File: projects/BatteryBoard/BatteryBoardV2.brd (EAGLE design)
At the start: 90.5 x 96 mm, 220 parts, among them M1 BSO201SP, SW1 BTS50015-1TAD, SW2 BTS50015-1TAD, T1 AD590FLATPACK, T2 AD590FLATPACK, T3 AD590FLATPACK, T4 AD590FLATPACK, U1 TCA9535PWR, U10 LT1962-3, U11 LT1962-3, U12 LTC4411, U13 LTC4411, U14 LTC4121, U15 VNS3NV04DP-E, U16 LTC4121, U17 VNS3NV04DP-E, U18 AD8418, U19 AD8418, U2 AD7991-0, U3 LTC4412MPS6, U4 LTC4121-4.2, U5 LTC4121-4.2, U6 LC05111C13MTTTG, U7 LC05111C13MTTTG, U8 AD8418, U9 AD8418

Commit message: Addition of zener diodes. Updates to some resistor values. Inital layout of all Li-ion circuitry.
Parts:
- removed V32: L2_ST, BrownSpaceEngineering:VIA-60MIL
- added D4, D5: SMBJ5343B, BattBoard:DO214AA
- added V40: LFB1SNS, BrownSpaceEngineering:VIA-60MIL
- added V44: LFB2SNS, BrownSpaceEngineering:VIA-60MIL
- R39: value 150K -> 15K
- R40: value 100K -> 10K
- R41, R59: value 0.002R@1W -> 0.001R@1W
- R42, R43, R60, R61: value 10K -> 470K
- R56, R57, R74, R75: value 10K -> 100K
- V31: value L1_ST -> L2_REF
- V33: value L_OUT -> L2_CHG; device BrownSpaceEngineering:VIA-120MIL -> BrownSpaceEngineering:VIA-60MIL
- V53: value LIFE_B2 -> LF_B2
- moved U19 237.8 mm to (86.7, 102.4), turned to 270 degrees
- moved R29 234.7 mm to (83.2, 102.1), turned to 270 degrees
- moved R30 230.3 mm to (83.2, 98.4), turned to 270 degrees
- moved R24 225.4 mm to (94.4, 85.7), turned to 270 degrees
- moved U18 225.3 mm to (99.1, 81.6), turned to 270 degrees
- moved R26 221.4 mm to (94.4, 82.0), turned to 270 degrees
- moved F1 174.5 mm to (29.8, 7.00), flipped to the bottom
- moved V42 164.5 mm to (101.3, 29.9)
- moved R8 151.8 mm to (-0.10, 73.5), flipped to the bottom, turned to 180 degrees
- moved V21 150.9 mm to (53.9, 4.60)
- moved R9 150.3 mm to (6.50, 14.1), turned to 180 degrees
- moved C13 149.7 mm to (-3.40, 79.5), flipped to the bottom, turned to 180 degrees
- moved R4 149.7 mm to (9.90, 68.5), turned to 90 degrees
- moved U6 148.2 mm to (0.80, 77.6), flipped to the bottom
- moved V20 147.8 mm to (47.9, 6.50), turned to 270 degrees
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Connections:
- net LIFE_B2 renamed LF_B2
- new net LFB1_SNS+: LIFEPO42.MINUS, R41.P$2, U18.P$8
- new net LFB2_SNS+: LIFEPO44.MINUS, R59.P$2, U19.P$8
- net GND: now also D4.A, D5.A
- net L1_SNS+: no longer LIFEPO42.MINUS, LIFEPO44.MINUS, R41.P$2, R59.P$2, U18.P$8, U19.P$8
- net L1_ST: no longer V31.P$1
- net L2_CHG: now also V33.P$1
- net L2_REF: now also V31.P$1
- net L2_ST: no longer V32.P$1
- net LF_B1_SNS: now also V40.P$1
- net LF_B2_SNS: now also V44.P$1
- net LIFE1: now also D4.C
- net LIFE3: now also D5.C
- net L_OUT: no longer V33.P$1

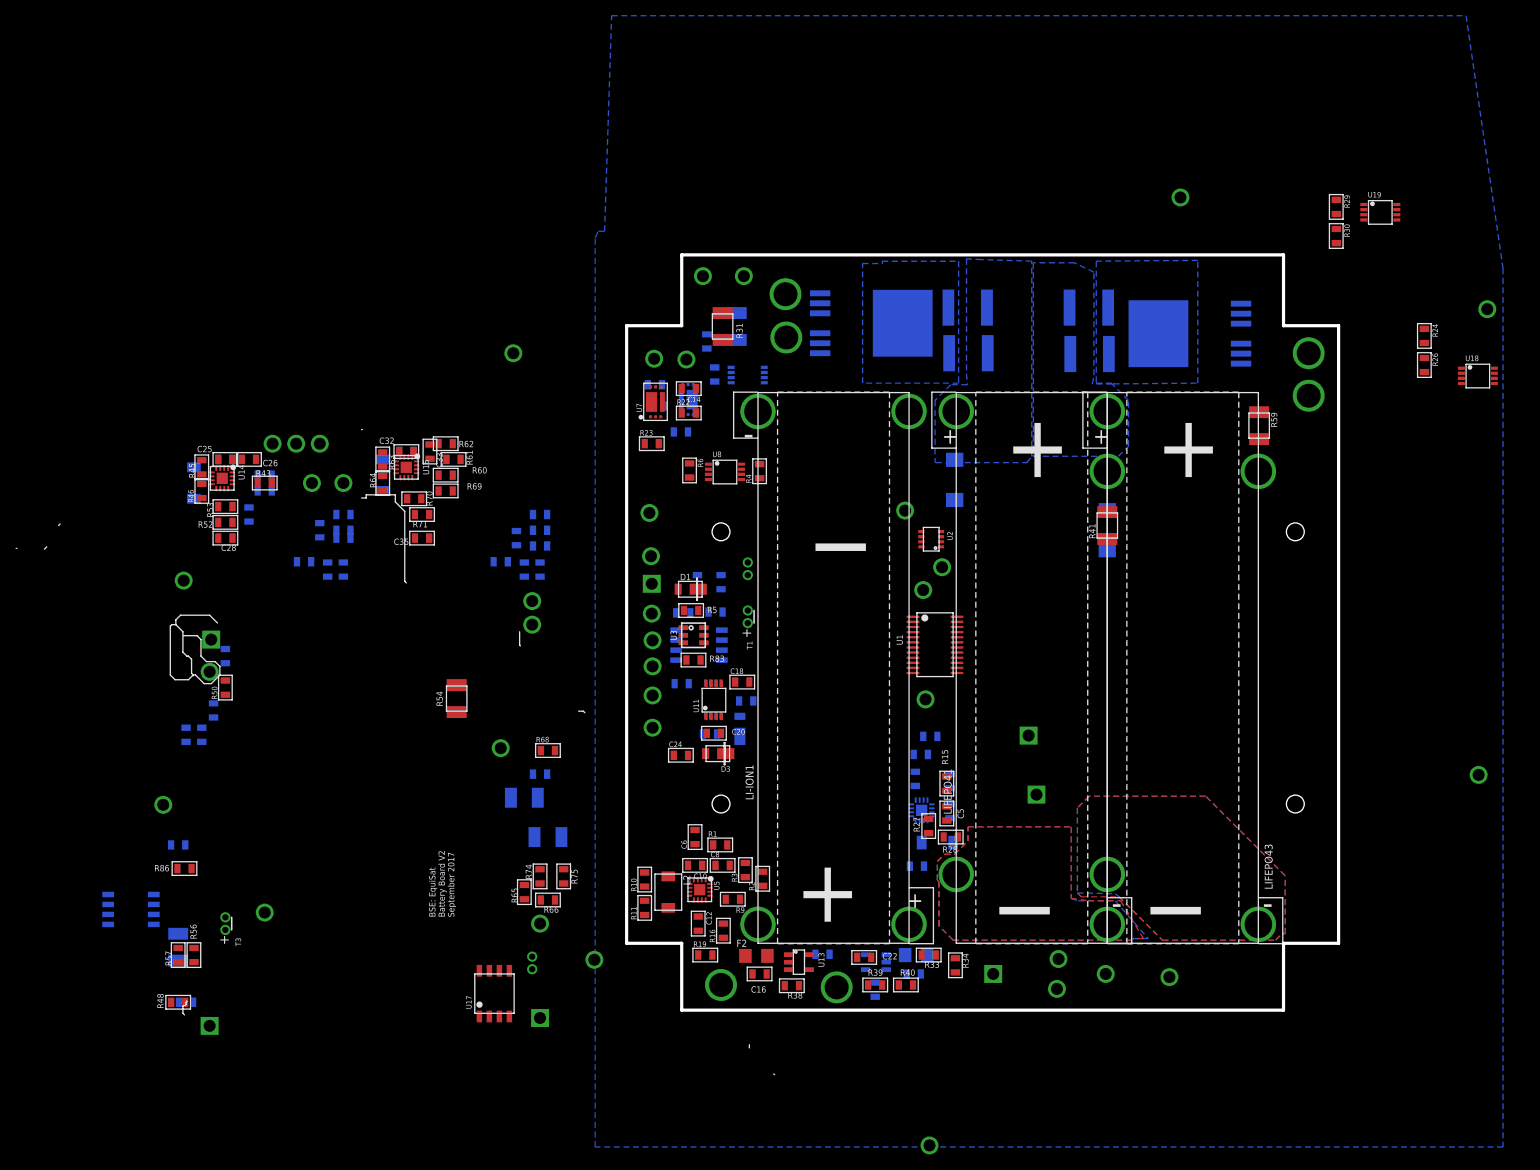
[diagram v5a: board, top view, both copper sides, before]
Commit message: Finished inital placement of all components on the battery board. Updated pull-down values for high-side switch input resistor.
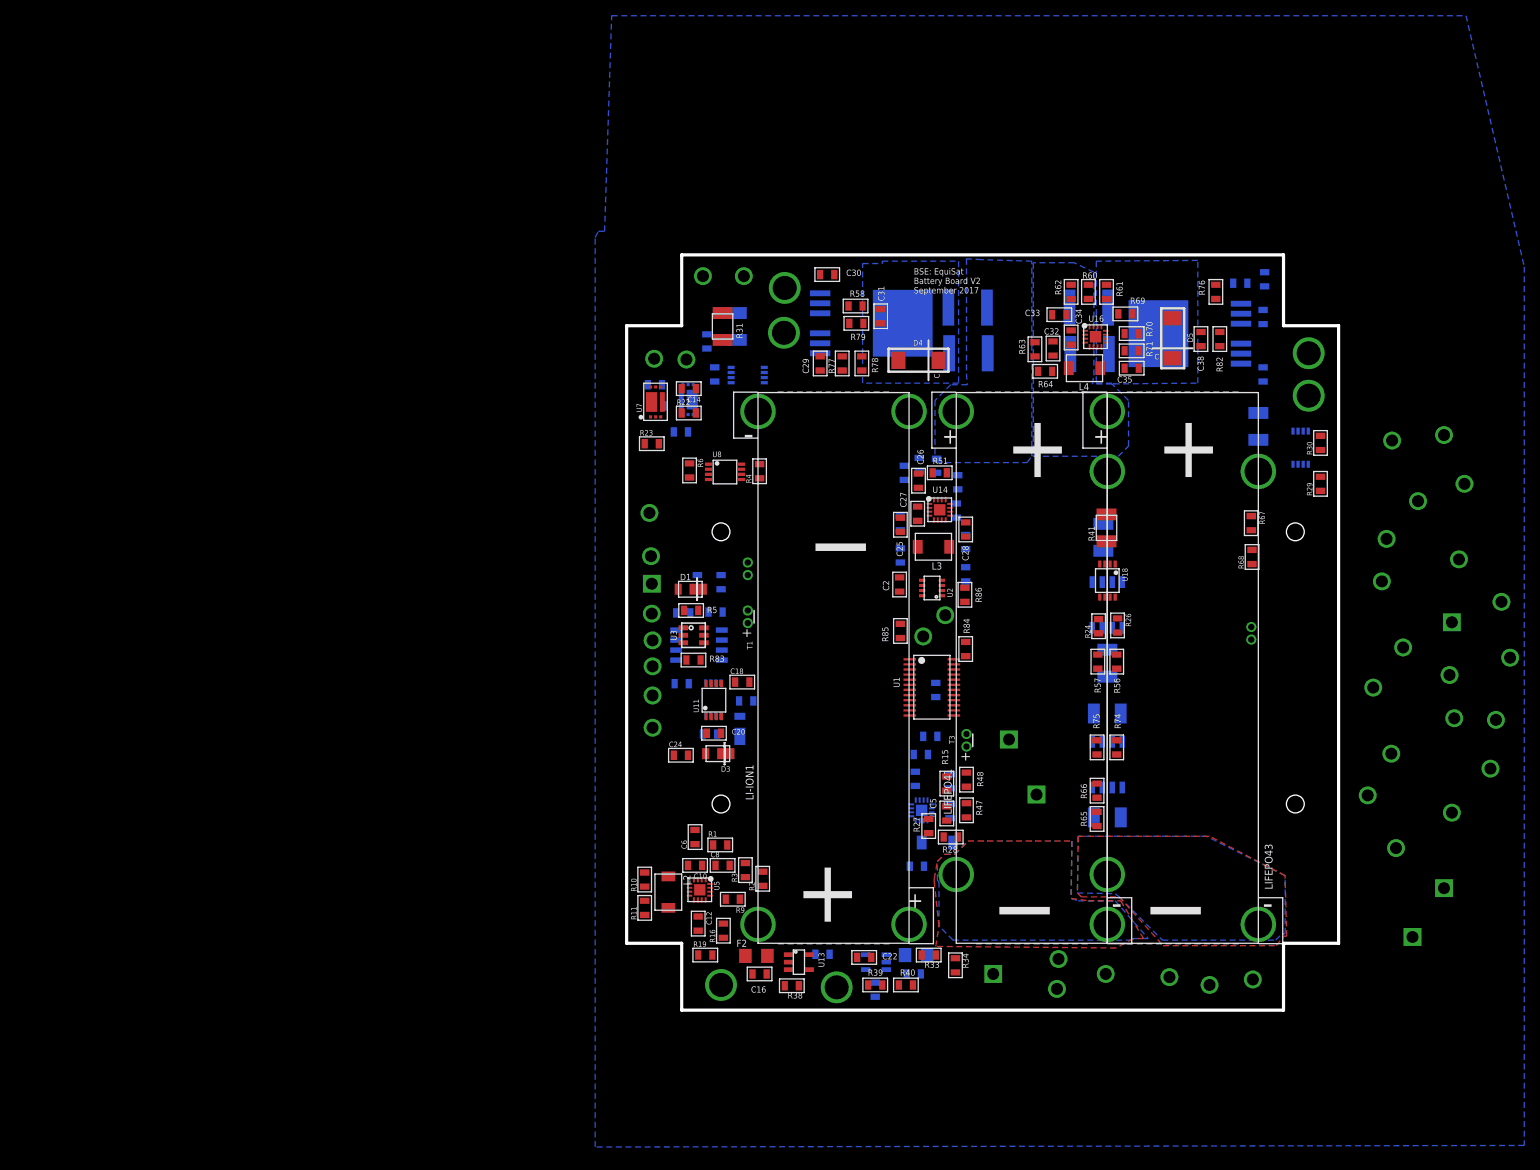
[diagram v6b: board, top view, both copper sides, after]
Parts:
- R77, R80: value 1K -> 100K
- R84: value 10K -> 1M
- moved V12 164.3 mm to (97.6, 42.6)
- moved V38 157.7 mm to (97.9, 49.3)
- moved V37 157.3 mm to (102.8, 30.7)
- moved V43 153.9 mm to (105.3, 44.8)
- moved V39 153.3 mm to (92.9, 9.30)
- moved V30 152.3 mm to (89.0, 54.5)
- moved V41 151.7 mm to (91.7, 46.1)
- moved V10 151.4 mm to (97.9, 25.1)
- moved V36 148.4 mm to (98.2, 37.1)
- moved V46 148.0 mm to (104.2, 51.9)
- moved V35 142.1 mm to (89.6, 59.9)
- moved U15 130.0 mm to (54.1, 51.5), turned to 0 degrees
- moved R55 123.5 mm to (54.1, 44.1)
- moved R56 123.1 mm to (55.3, 44.3), turned to 90 degrees
- moved V47 123.0 mm to (98.8, 57.3)
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
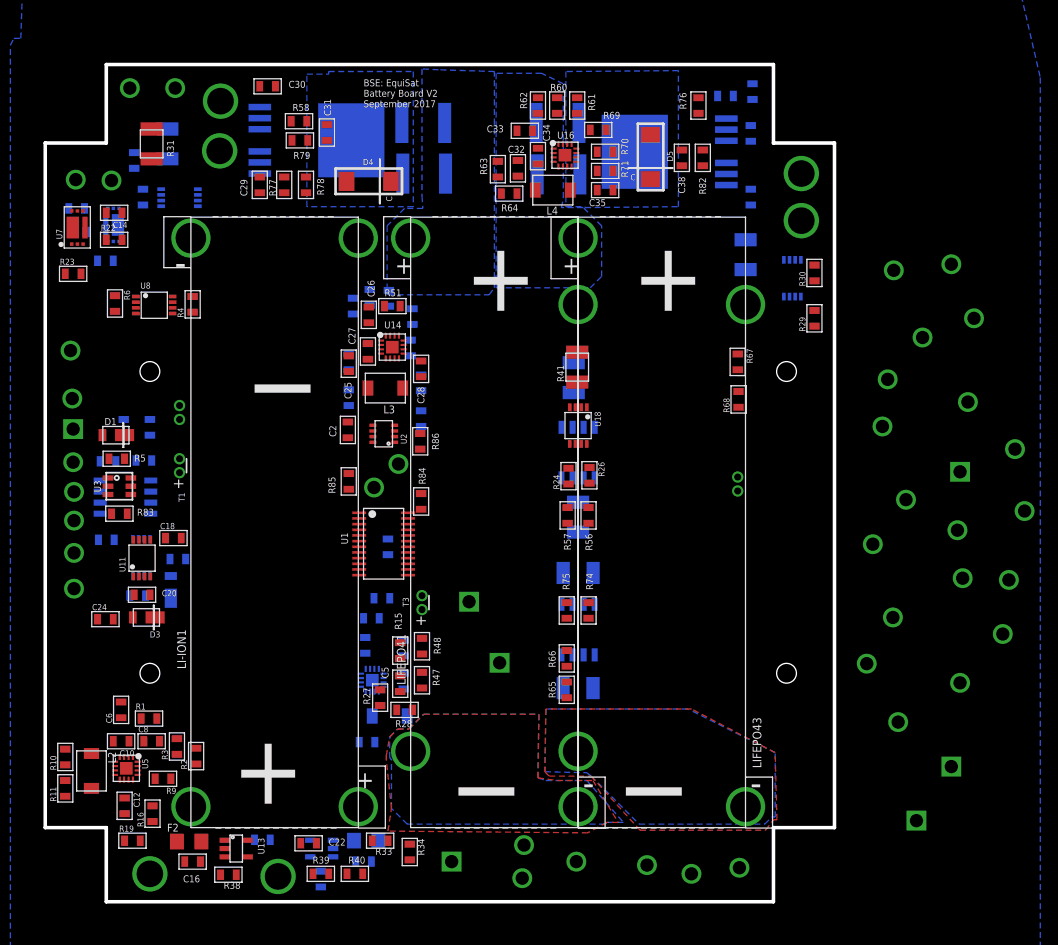
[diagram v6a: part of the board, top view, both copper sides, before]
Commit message: Continued routing of Battery Board V2. Addition of a few extra debugging vias. Addition of resistor dividers on li-ion charge commands.
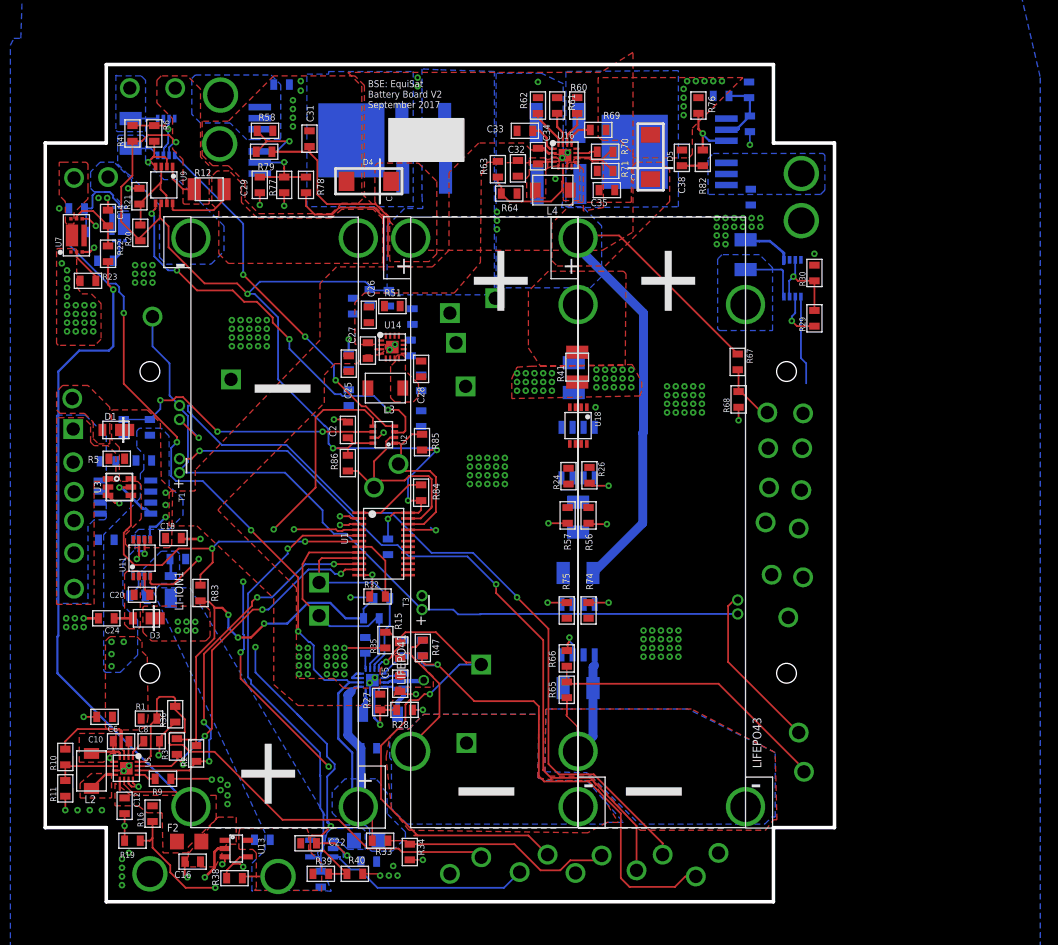
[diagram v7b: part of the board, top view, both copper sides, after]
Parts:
- removed V28: LION1_OUT, BrownSpaceEngineering:VIA-60MIL-SQ
- added R32, R35, R36: 100K, BrownSpaceEngineering:0805
- added V32: LF_B1_CHG, BrownSpaceEngineering:VIA-60MIL-SQ
- added V48: L1_CHG, BrownSpaceEngineering:VIA-60MIL-SQ
- R1, R15: value 10K -> 40.9K
- V36, V37: device BrownSpaceEngineering:VIA-60MIL -> BrownSpaceEngineering:VIA-60MIL-SQ
- moved V3 93.8 mm to (14.3, 59.9)
- moved V30 71.4 mm to (39.4, 3.20)
- moved V37 67.8 mm to (41.2, 59.1), turned to 180 degrees
- moved V36 64.1 mm to (40.1, 64.1)
- moved V38 56.9 mm to (44.6, 69.2)
- moved V39 52.4 mm to (41.3, 18.2)
- moved V42 49.4 mm to (67.6, 2.90)
- moved V29 46.7 mm to (47.4, 3.40), turned to 180 degrees
- moved V10 33.9 mm to (70.2, 5.60), turned to 270 degrees
- moved V40 32.2 mm to (76.3, 37.5), turned to 270 degrees
- moved $6_188_$_2017-09-09_23-53-10 29.8 mm to (75.9, 52.0), turned to 180 degrees
- moved V46 28.5 mm to (76.0, 47.5)
- moved V49 27.6 mm to (75.8, 56.1)
- moved V50 27.3 mm to (80.0, 14.9), turned to 90 degrees
- moved V43 26.5 mm to (79.9, 37.2), turned to 270 degrees
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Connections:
- new net N$15: R32.2, U1.P$7
- net GND: now also R32.1, R35.1, R36.1
- net L1_CHG: now also R35.2, V48.P$1
- net L2_CHG: now also R36.2
- net LF_B1_CHG: now also V32.P$1
- net LION1_OUT: no longer V28.P$1
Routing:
- net +3V3: track 0.00 -> 183.5 mm, vias 0 -> 11
- net GND: track 0.00 -> 118.9 mm, vias 0 -> 271
- net LION1: track 0.00 -> 106.4 mm, vias 0 -> 4
- net L2_TEMP: track 0.00 -> 94.0 mm, vias 0 -> 2
- net 5V: track 0.00 -> 91.5 mm
- net L1_TEMP: track 0.00 -> 85.1 mm, vias 0 -> 2
- net LION2: track 0.00 -> 84.2 mm, vias 0 -> 1
- net L_REF: track 0.00 -> 75.1 mm, vias 0 -> 3
- net LIFE3: track 0.00 -> 68.0 mm
- net L2_ST: track 0.00 -> 67.5 mm, vias 0 -> 5
- net L1_CHG: track 0.00 -> 63.4 mm, vias 0 -> 2
- net L2_REF: track 0.00 -> 59.8 mm, vias 0 -> 1
- net L2_CHG: track 0.00 -> 59.4 mm
- net LF2_REF: track 0.00 -> 55.1 mm, vias 0 -> 1
- net L1_ST: track 0.00 -> 54.2 mm, vias 0 -> 1
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- added copper zone on layer 1, net GND
- added copper zone on layer 16, net L1_SNS+
- added copper zone on layer 16, net L1_SNS-
- added copper zone on layer 1, net L2_SNS+
- added copper zone on layer 1, net L2_SNS-
- added copper zone on layer 1, net LFB1_SNS+
- added copper zone on layer 16, net LFB2_SNS+
- added copper zone on layer 16, net LF_B1
- added copper zone on layer 16, net LF_B2
- added copper zone on layer 1, net LIFE1
- added copper zone on layer 1, net LIFE3
- added copper zone on layer 16, net LION1
- added copper zone on layer 16, net LION1_OUT
- added copper zone on layer 1, net LION2
- added copper zone on layer 1, net LION2_OUT
- added copper zone on layer 1, net L_OUT
- added copper zone on layer 16, net L_OUT
- added copper zone on layer 16, net N$16
- added copper zone on layer 1, net N$2
- added copper zone on layer 16, net N$3
- added copper zone on layer 1, net N$32
- added copper zone on layer 1, net N$39
- added copper zone on layer 1, net N$41
- added copper zone on layer 1, net N$49
- added copper zone on layer 1, net N$52
- added copper zone on layer 1, net N$6
- added copper zone on layer 1, net SP_C
- added copper zone on layer 16, net SP_C
- added copper zone on layer 1, net SP_OUT
- added copper zone on layer 16, net SP_OUT
- added copper zone on layer 1, net UMB_CHG
